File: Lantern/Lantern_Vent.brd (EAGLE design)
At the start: 82 x 82 mm, 9 parts

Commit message: Fixed Resistors
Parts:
- moved R1 4.60 mm to (-4.00, -22.0)
- moved R2 4.60 mm to (0.00, -22.0)
- moved R3 4.60 mm to (4.00, -22.0)
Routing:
- net VCC: track 84.2 -> 99.4 mm, vias 2 -> 5
- net N$2: track 65.3 -> 60.5 mm
- net N$3: track 17.5 -> 12.9 mm
- net N$1: track 18.3 -> 14.7 mm
- net GND: vias 121 -> 118
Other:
- board text added: "PCB Bottle-Lantern"
- board text added: "ripper121.com"
- board text removed: "bottle-lantern.com"
- board text removed: "ripper121"

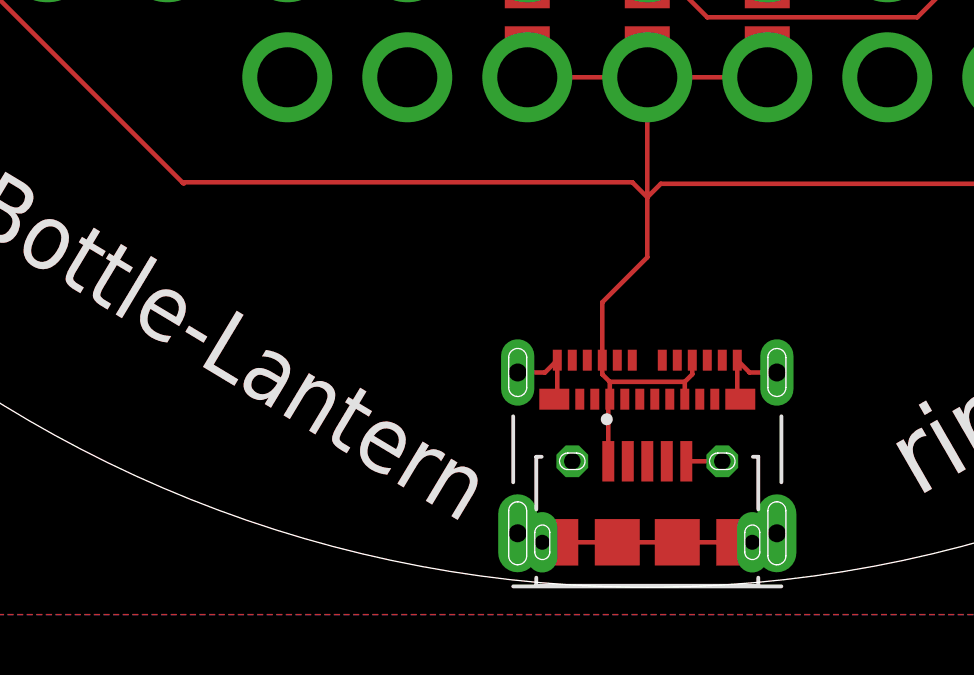
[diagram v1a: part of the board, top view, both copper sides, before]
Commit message: DRC fix
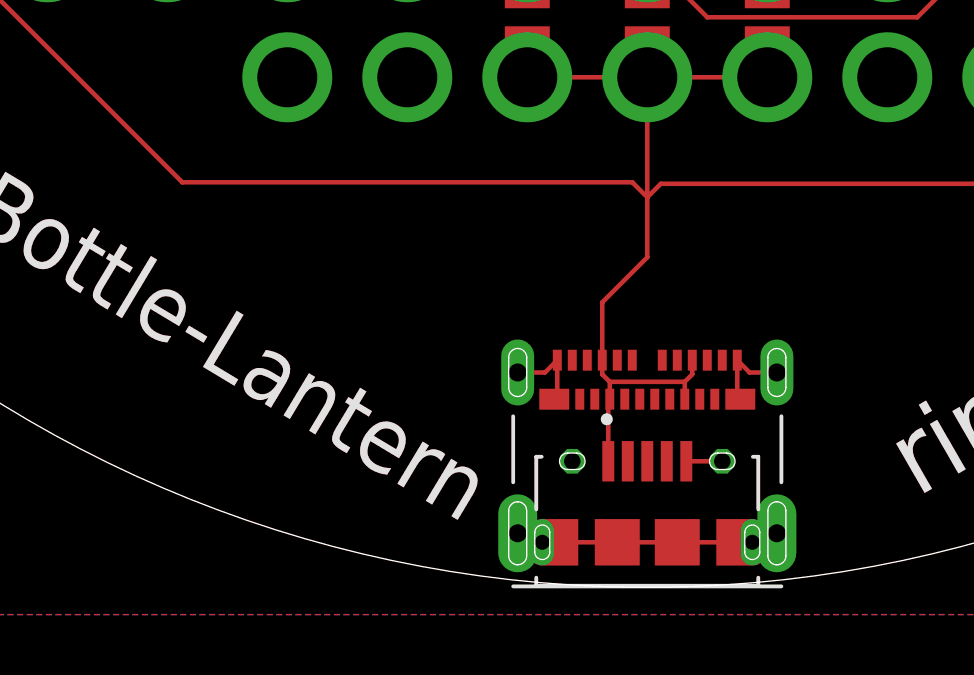
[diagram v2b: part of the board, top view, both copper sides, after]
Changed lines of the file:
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@@
 </layers>
 <board>
-<fusionsync huburn="a.YnVzaW5lc3M6YWlwaWxvdA" projecturn="a.YnVzaW5lc3M6YWlwaWxvdCMyMDIxMDEwNTM2ODY3ODk4MQ" f3durn="urn:adsk.wipprod:dm.lineage:4nC3t7VVRIajsZ478DbCBA" pcbguid="" lastpulledtime="" lastsyncedchangeguid="" latestrevisionid="ed4cb2aa-e272-4962-b348-96793fb0dd4e" lastsyncedrevisionid="ed4cb2aa-e272-4962-b348-96793fb0dd4e" lastboardhashguid="29032e68-1f9e-31bd-33ff-1babf3852947" lastpushedtime="2021-01-15T13:54:04Z" linktopcb3d="true"/>
+<fusionsync huburn="a.YnVzaW5lc3M6YWlwaWxvdA" projecturn="a.YnVzaW5lc3M6YWlwaWxvdCMyMDIxMDEwNTM2ODY3ODk4MQ" f3durn="urn:adsk.wipprod:dm.lineage:4nC3t7VVRIajsZ478DbCBA" pcbguid="" lastpulledtime="" lastsyncedchangeguid="" latestrevisionid="5e2d3c63-fdda-4a7c-a73d-e5daa198b441" lastsyncedrevisionid="5e2d3c63-fdda-4a7c-a73d-e5daa198b441" lastboardhashguid="d56f2985-82f6-c8f6-bcbf-6046cd75418d" lastpushedtime="2021-01-15T22:17:48Z" linktopcb3d="true"/>
 <plain>
 <circle x="0" y="0" radius="41" width="0.001" layer="20"/>
@@
 </class>
 </classes>
-<designrules name="default">
-<description language="de">&lt;b&gt;EAGLE Design Rules&lt;/b&gt;
+<designrules name="jlcpcb2layer *">
+<description language="en">&lt;b&gt;JLCPCB Design Rules by Jaap de Dood&lt;/b&gt;
 &lt;p&gt;
-Die Standard-Design-Rules sind so gewählt, dass sie für
-die meisten Anwendungen passen. Sollte ihre Platine
-besondere Anforderungen haben, treffen Sie die erforderlichen
-Einstellungen hier und speichern die Design Rules unter
-einem neuen Namen ab.</description>
-<description language="en">&lt;b&gt;EAGLE Design Rules&lt;/b&gt;
-&lt;p&gt;
-The default Design Rules have been set to cover
-a wide range of applications. Your particular design
-may have different requirements, so please make the
-necessary adjustments and save your customized
-design rules under a new name.</description>
+Please make sure your boards conform to these design rules.
+&lt;/p&gt;</description>
 <param name="layerSetup" value="(1*16)"/>
-<param name="mtCopper" value="0.035mm 0.035mm 0.035mm 0.035mm 0.035mm 0.035mm 0.035mm 0.035mm 0.035mm 0.035mm 0.035mm 0.035mm 0.035mm 0.035mm 0.035mm 0.035mm"/>
-<param name="mtIsolate" value="1.5mm 0.15mm 0.2mm 0.15mm 0.2mm 0.15mm 0.2mm 0.15mm 0.2mm 0.15mm 0.2mm 0.15mm 0.2mm 0.15mm 0.2mm"/>
-<param name="mdWireWire" value="6mil"/>
-<param name="mdWirePad" value="6mil"/>
-<param name="mdWireVia" value="6mil"/>
-<param name="mdPadPad" value="6mil"/>
-<param name="mdPadVia" value="6mil"/>
-<param name="mdViaVia" value="6mil"/>
-<param name="mdSmdPad" value="6mil"/>
-<param name="mdSmdVia" value="6mil"/>
-<param name="mdSmdSmd" value="6mil"/>
-<param name="mdViaViaSameLayer" value="6mil"/>
+<param name="mtCopper" value="0.035559375mm 0.0356mm 0.0356mm 0.0356mm 0.0356mm 0.0356mm 0.0356mm 0.0356mm 0.0356mm 0.0356mm 0.0356mm 0.0356mm 0.0356mm 0.0356mm 0.0356mm 0.035559375mm"/>
+<param name="mtIsolate" value="1.6mm 0.1499mm 0.2007mm 0.1499mm 0.2007mm 0.1499mm 0.2007mm 0.1499mm 0.2007mm 0.1499mm 0.2007mm 0.1499mm 0.2007mm 0.1499mm 0.2007mm"/>
+<param name="mdWireWire" value="5mil"/>
+<param name="mdWirePad" value="5mil"/>
+<param name="mdWireVia" value="20mil"/>
+<param name="mdPadPad" value="5mil"/>
+<param name="mdPadVia" value="5mil"/>
+<param name="mdViaVia" value="5mil"/>
+<param name="mdSmdPad" value="5mil"/>
+<param name="mdSmdVia" value="5mil"/>
+<param name="mdSmdSmd" value="5mil"/>
+<param name="mdViaViaSameLayer" value="8mil"/>
 <param name="mnLayersViaInSmd" value="2"/>
-<param name="mdCopperDimension" value="40mil"/>
+<param name="mdCopperDimension" value="8mil"/>
 <param name="mdDrill" value="6mil"/>
 <param name="mdSmdStop" value="0mil"/>
-<param name="msWidth" value="6mil"/>
-<param name="msDrill" value="0.35mm"/>
-<param name="msMicroVia" value="9.99mm"/>
+<param name="msWidth" value="5mil"/>
+<param name="msDrill" value="12mil"/>
+<param name="msMicroVia" value="12mil"/>
 <param name="msBlindViaRatio" value="0.5"/>
 <param name="rvPadTop" value="0.25"/>
@@
 <param name="rvMicroViaOuter" value="0.25"/>
 <param name="rvMicroViaInner" value="0.25"/>
-<param name="rlMinPadTop" value="10mil"/>
+<param name="rlMinPadTop" value="5mil"/>
 <param name="rlMaxPadTop" value="20mil"/>
-<param name="rlMinPadInner" value="10mil"/>
+<param name="rlMinPadInner" value="5mil"/>
 <param name="rlMaxPadInner" value="20mil"/>
-<param name="rlMinPadBottom" value="10mil"/>
+<param name="rlMinPadBottom" value="5mil"/>
 <param name="rlMaxPadBottom" value="20mil"/>
-<param name="rlMinViaOuter" value="8mil"/>
+<param name="rlMinViaOuter" value="3mil"/>
 <param name="rlMaxViaOuter" value="20mil"/>
-<param name="rlMinViaInner" value="8mil"/>
+<param name="rlMinViaInner" value="3mil"/>
 <param name="rlMaxViaInner" value="20mil"/>
-<param name="rlMinMicroViaOuter" value="4mil"/>
+<param name="rlMinMicroViaOuter" value="3mil"/>
 <param name="rlMaxMicroViaOuter" value="20mil"/>
-<param name="rlMinMicroViaInner" value="4mil"/>
+<param name="rlMinMicroViaInner" value="3mil"/>
 <param name="rlMaxMicroViaInner" value="20mil"/>
 <param name="psTop" value="-1"/>
@@
 <param name="mvStopFrame" value="1"/>
 <param name="mvCreamFrame" value="0"/>
-<param name="mlMinStopFrame" value="4mil"/>
-<param name="mlMaxStopFrame" value="4mil"/>
+<param name="mlMinStopFrame" value="2.5mil"/>
+<param name="mlMaxStopFrame" value="2.5mil"/>
 <param name="mlMinCreamFrame" value="0mil"/>
 <param name="mlMaxCreamFrame" value="0mil"/>
@@
 <wire x1="25" y1="-18" x2="15.45" y2="-27.55" width="0.1524" layer="1"/>
 <via x="-31.2" y="-18" extent="1-16" drill="4.3" diameter="7.9"/>
-<wire x1="-15.45" y1="-27.55" x2="-15.5" y2="-27.5" width="0.1524" layer="1"/>
 <wire x1="-15.5" y1="-27.5" x2="-25" y2="-18" width="0.1524" layer="1"/>
 <wire x1="-25" y1="-18" x2="-31.2" y2="-18" width="0.1524" layer="1"/>

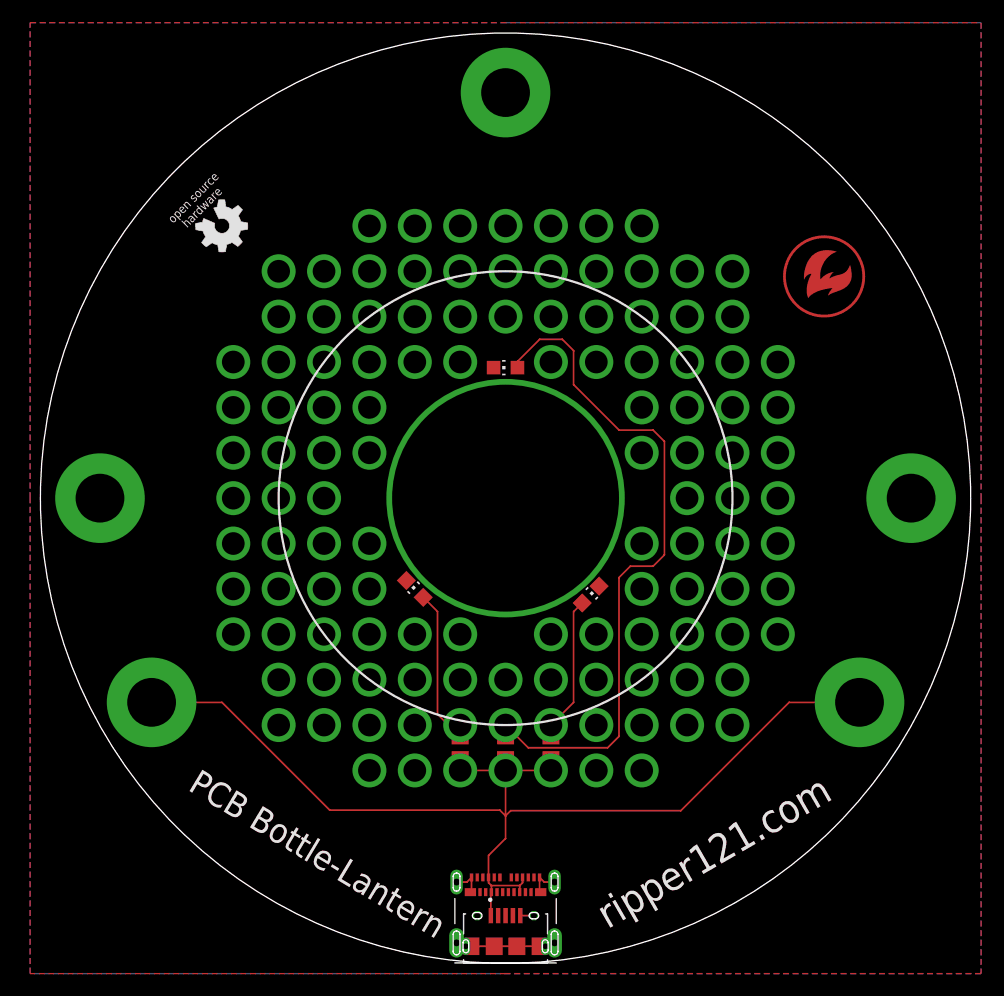
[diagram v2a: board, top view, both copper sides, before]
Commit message: Added Fuse
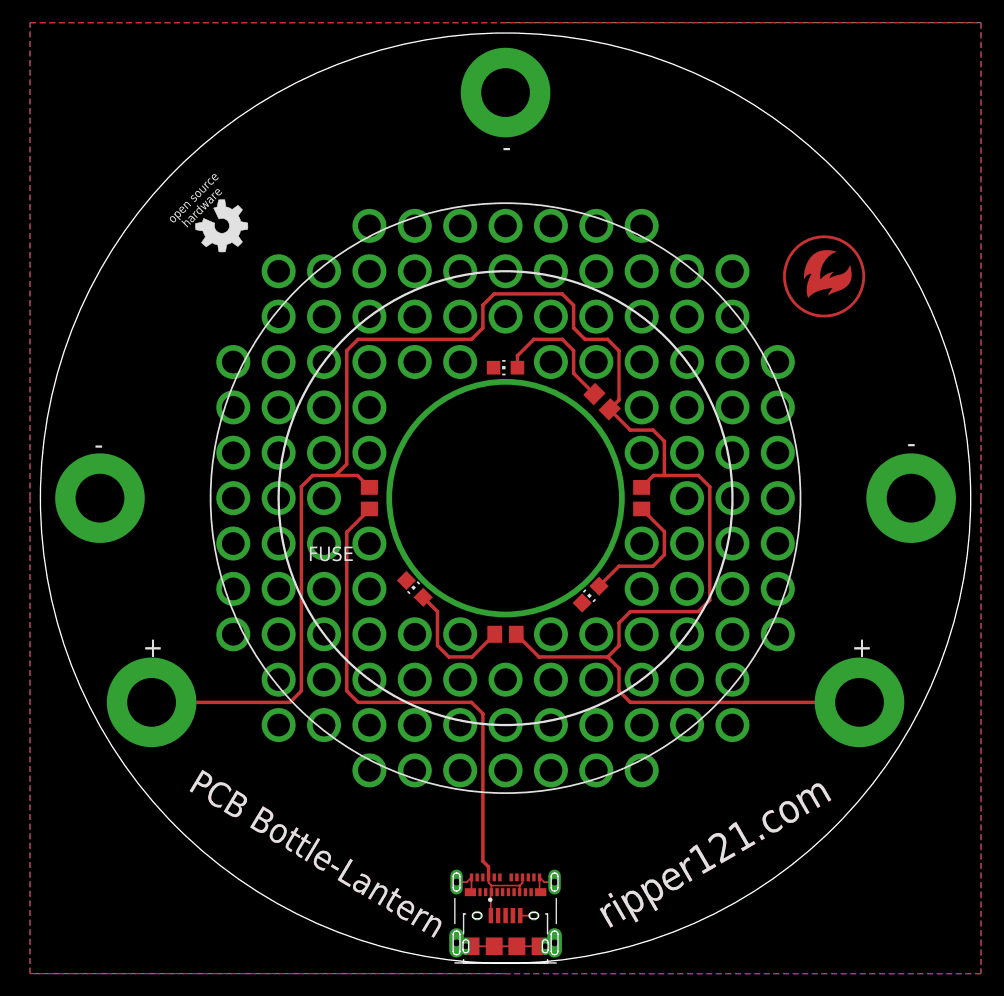
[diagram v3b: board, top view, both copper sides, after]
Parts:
- added FUSE: 10R, rcl:R0805
- R1, R2, R3: value (none) -> 120R
- moved R2 31.7 mm to (8.50, 8.50), turned to 135 degrees
- moved R3 23.4 mm to (12.0, 0.00), turned to 270 degrees
- moved R1 10.8 mm to (0.00, -12.0), turned to 180 degrees
- turned LED3 to 135 degrees
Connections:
- new net VCC_OUT: FUSE.2, R1.1, R2.1, R3.1
- net VCC: now also FUSE.1; no longer R1.1, R2.1, R3.1
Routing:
- net VCC_OUT: track 0.00 -> 157.9 mm, vias 0 -> 2
- net N$2: track 60.5 -> 11.6 mm, vias 1 -> 0
- net VCC: track 99.3 -> 51.7 mm, vias 5 -> 0
- net N$1: track 14.7 -> 11.1 mm, vias 1 -> 0
- net N$3: track 12.9 -> 11.8 mm, vias 1 -> 0
- net GND: vias 118 -> 124
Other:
- board text added: "+"
- board text added: "-"
